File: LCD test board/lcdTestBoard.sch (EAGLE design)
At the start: 71 parts, among them CON2 AXE534124, U1 LP2980-ADJ, U2 ST2378E_TSSOP, U3 MCP1662, U4 TPS62260, U5 ST2378E_TSSOP, U6 LP2980-ADJ, U7 TPS62260, U8 LP2980-ADJ, U9 TPS62260

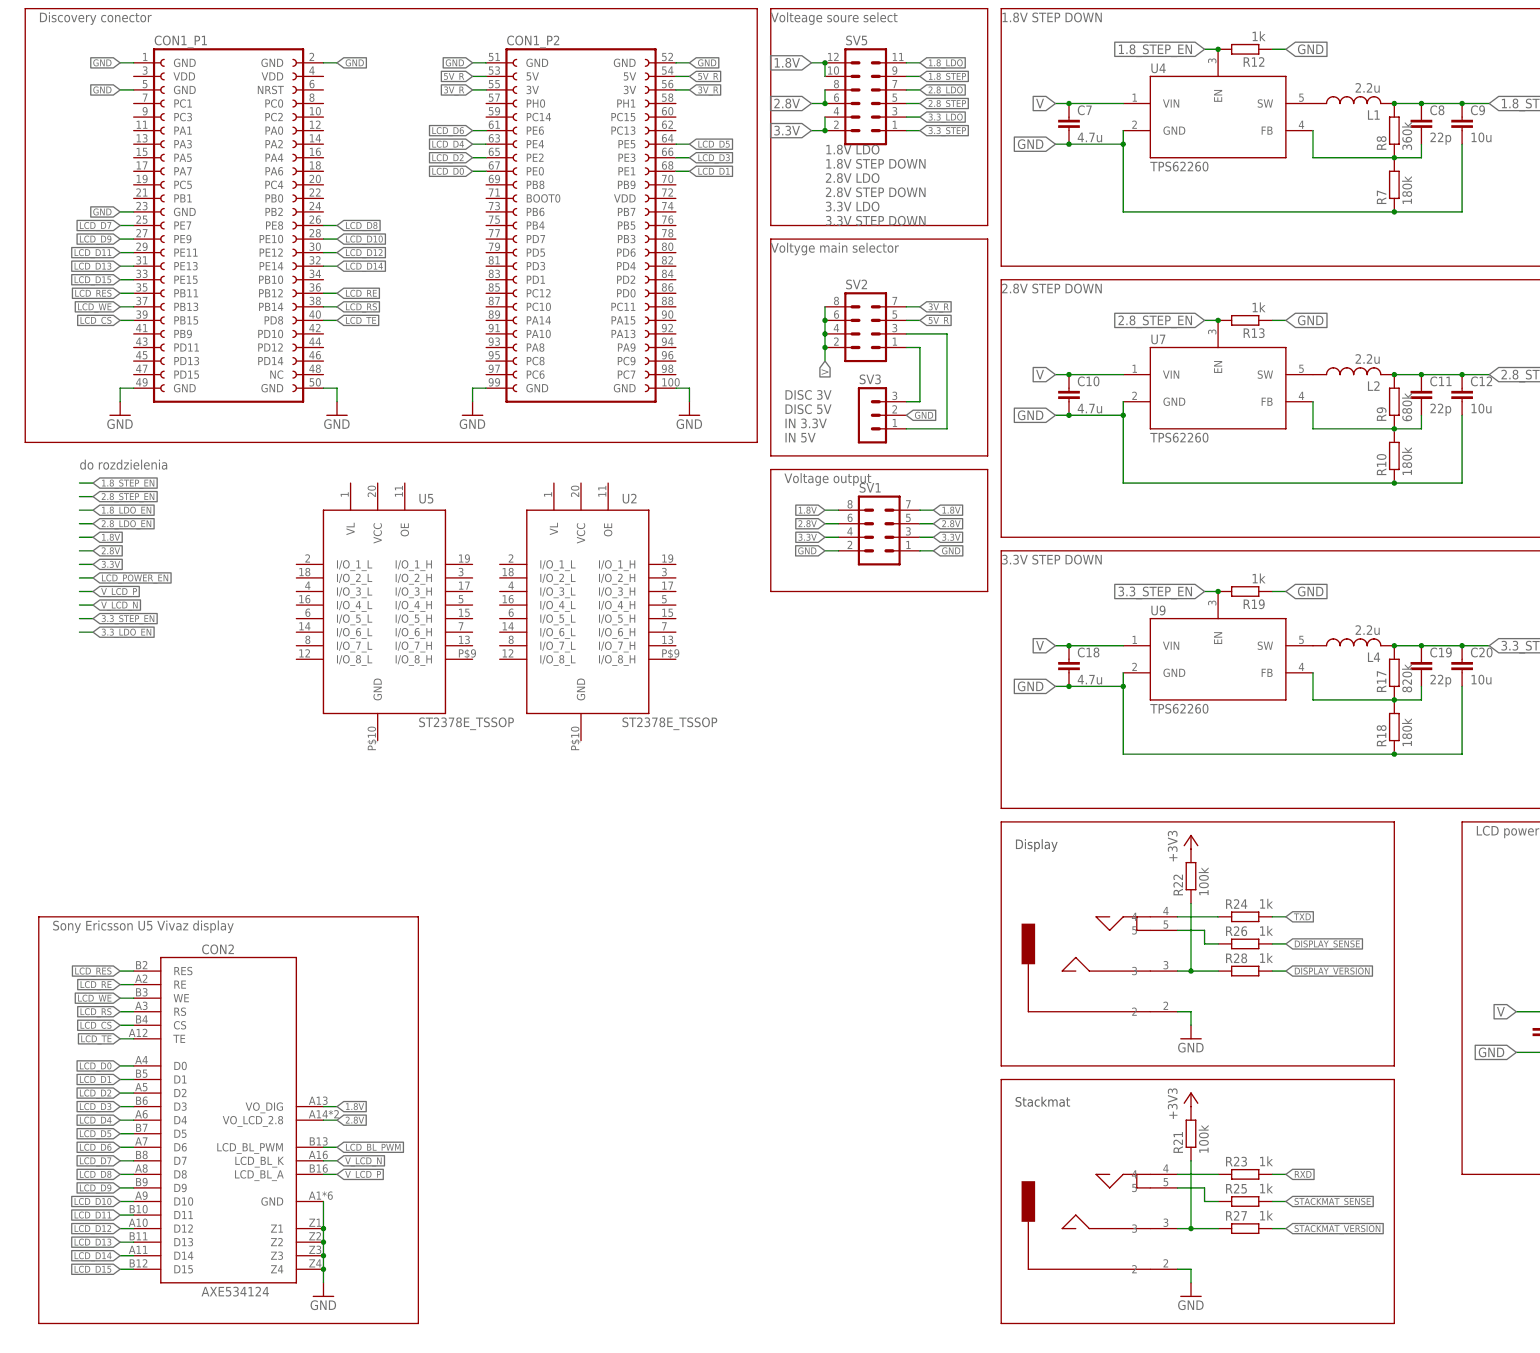
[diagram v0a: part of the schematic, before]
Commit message: polaczono wyswietlacz i stackmate do portu usart procesora, dodano invertery
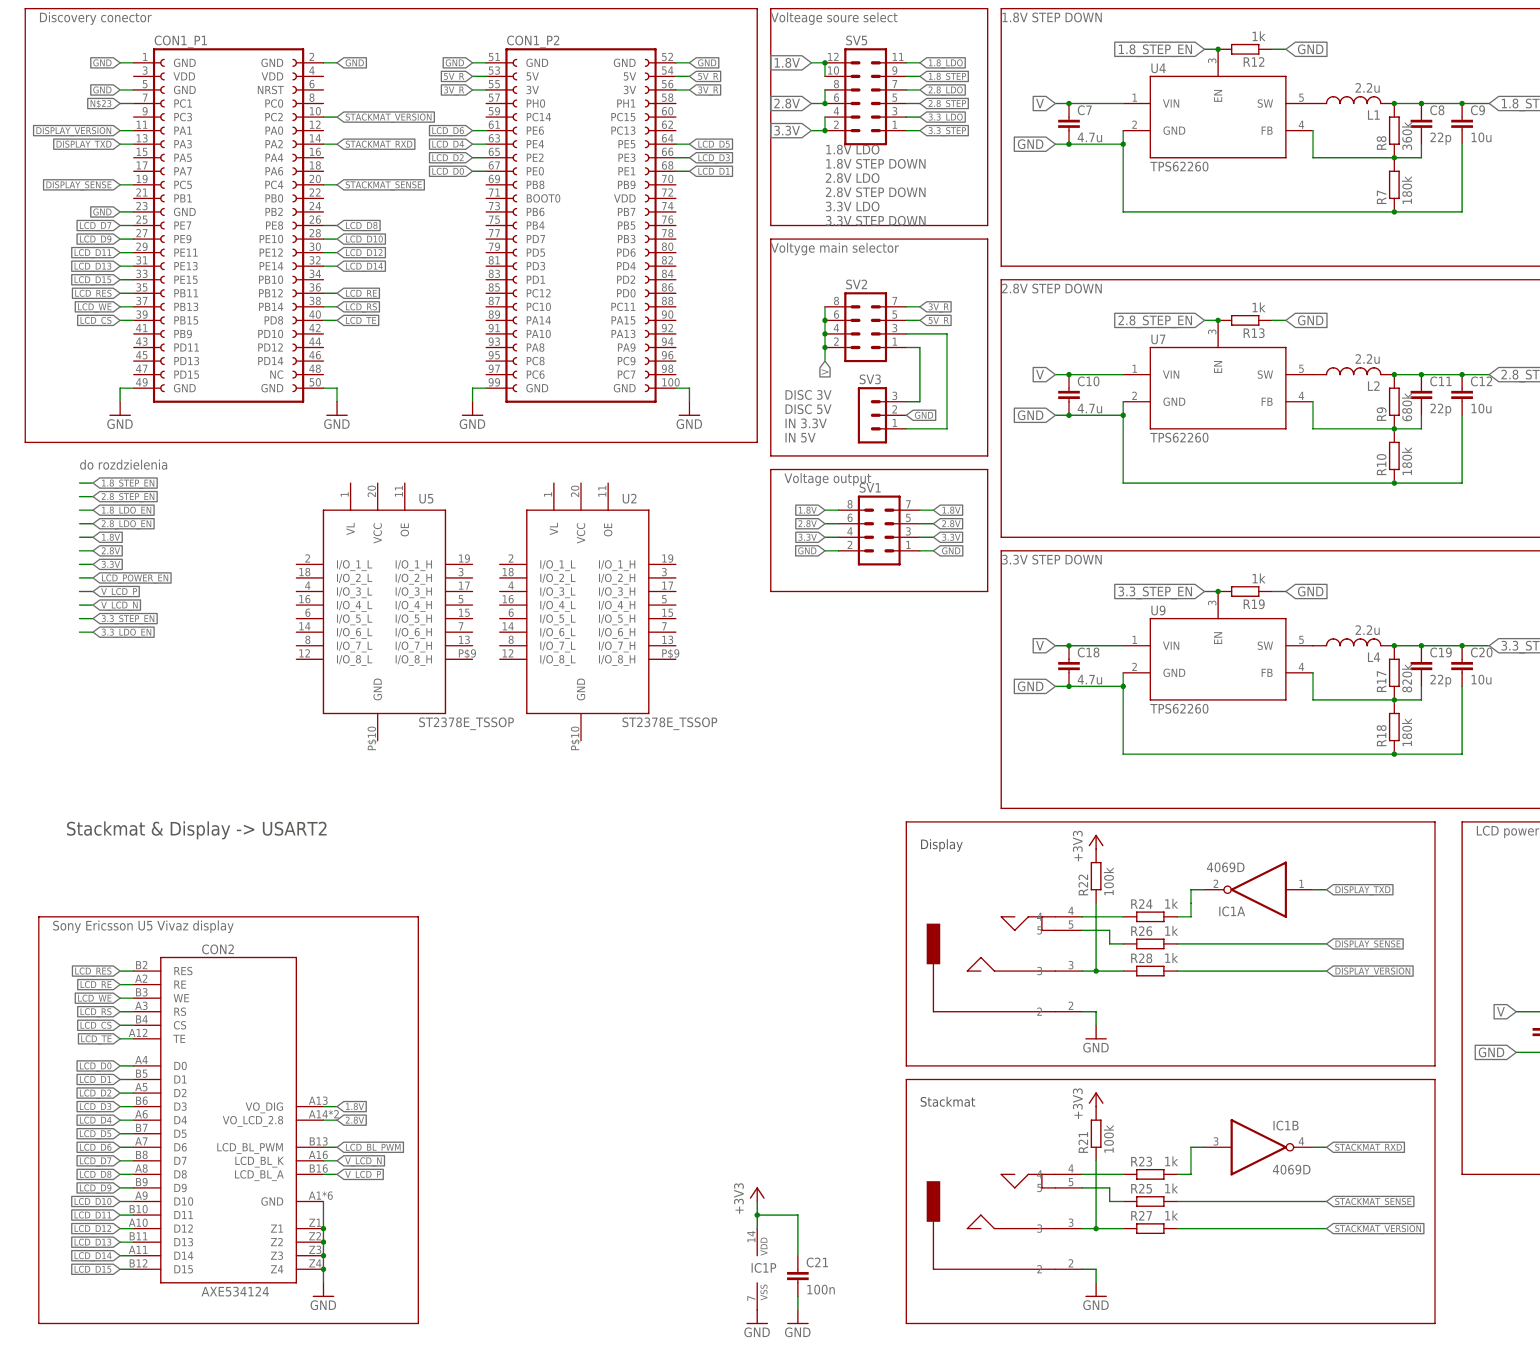
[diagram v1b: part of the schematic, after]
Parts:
- added C21: 100n, rcl:C-EUC0603K
- added IC1: 4069D, 40xx:4069D
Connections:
- removed net RXD: R23.1
- removed net TXD: R24.1
- new net DISPLAY_TXD: CON1_P1.PA3@13, IC1A.I
- new net N$20: IC1A.O, R24.1
- new net N$21: IC1B.I, R23.1
- new net N$23: CON1_P1.PC1@7
- new net STACKMAT_RXD: CON1_P1.PA2@14, IC1B.O
- net +3V3: now also C21.1, IC1P.VDD
- net DISPLAY_SENSE: now also CON1_P1.PC5@19
- net DISPLAY_VERSION: now also CON1_P1.PA1@11
- net GND: now also C21.2, IC1P.VSS
- net LCD_CS: now also CON1_P1.PB15@39
- net LCD_D0: now also CON1_P2.PE0@17
- net LCD_D1: now also CON1_P2.PE1@18
- net LCD_D10: now also CON1_P1.PE10@28
- net LCD_D11: now also CON1_P1.PE11@29
- net LCD_D12: now also CON1_P1.PE12@30
- net LCD_D13: now also CON1_P1.PE13@31
- net LCD_D14: now also CON1_P1.PE14@32
- net LCD_D15: now also CON1_P1.PE15@33
- net LCD_D2: now also CON1_P2.PE2@15
- net LCD_D3: now also CON1_P2.PE3@16
- net LCD_D4: now also CON1_P2.PE4@13
- net LCD_D5: now also CON1_P2.PE5@14
- net LCD_D6: now also CON1_P2.PE6@11
- net LCD_D7: now also CON1_P1.PE7@25
- net LCD_D8: now also CON1_P1.PE8@26
- net LCD_D9: now also CON1_P1.PE9@27
- net LCD_RE: now also CON1_P1.PB12@36
- net LCD_RES: now also CON1_P1.PB11@35
- net LCD_RS: now also CON1_P1.PB14@38
- net LCD_TE: now also CON1_P1.PD8@40
- net LCD_WE: now also CON1_P1.PB13@37
- net STACKMAT_SENSE: now also CON1_P1.PC4@20
- net STACKMAT_VERSION: now also CON1_P1.PC2@10
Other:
- note added: "Stackmat & Display -> USART2"
- moved on the sheet: R21, R22, R23, R24, R25, R26, R27, R28

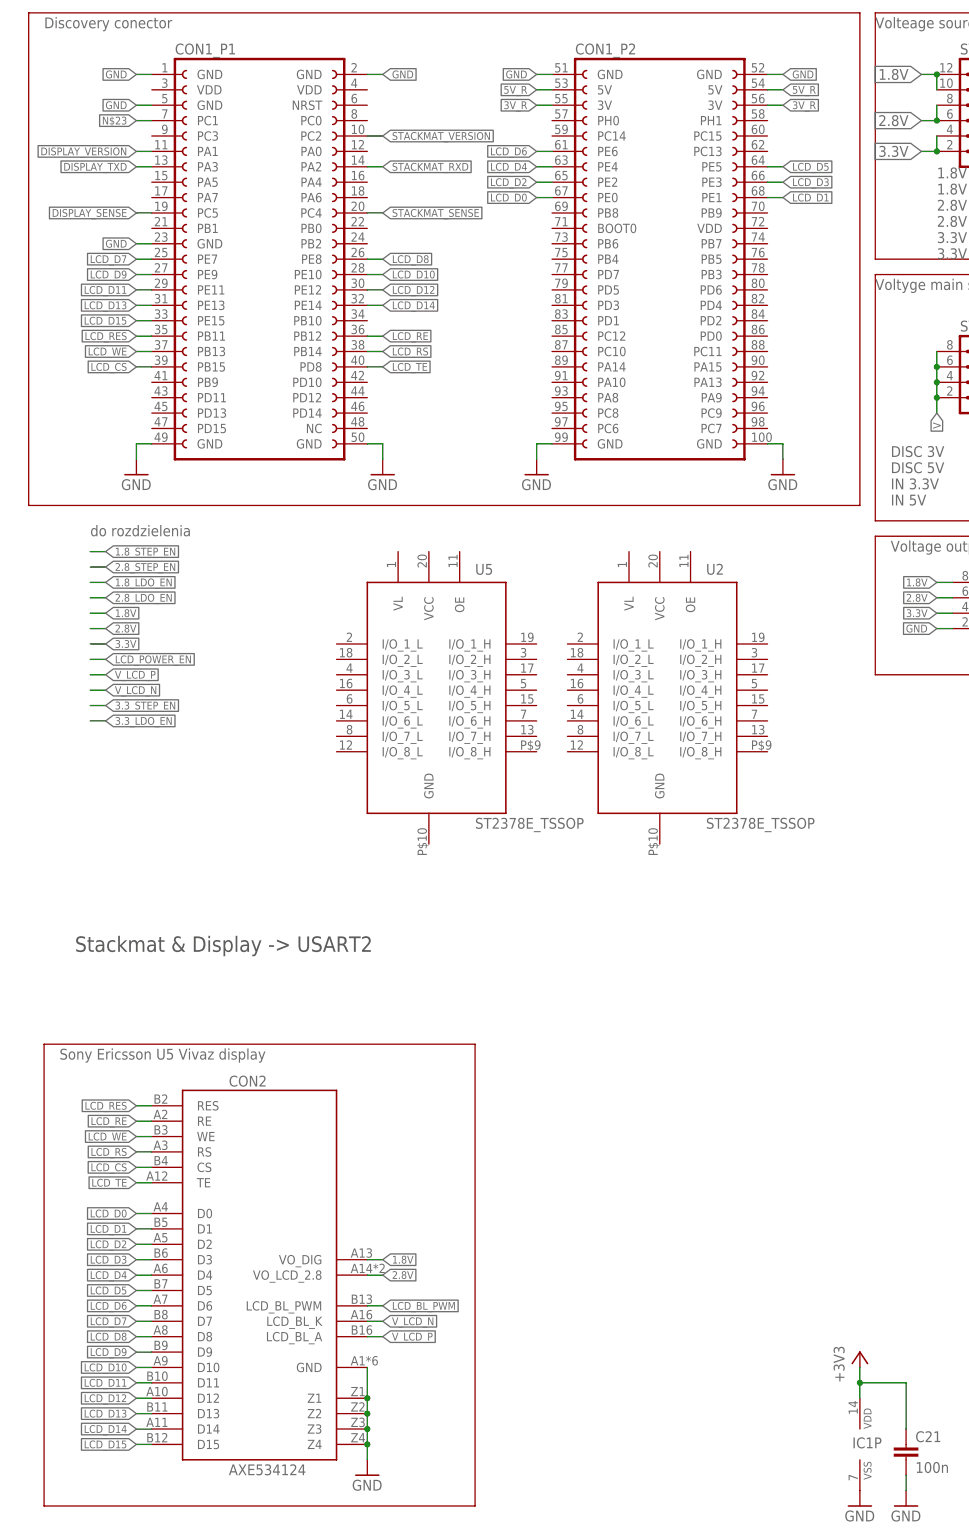
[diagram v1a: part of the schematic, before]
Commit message: dodano kondensatory przy złączu lcd
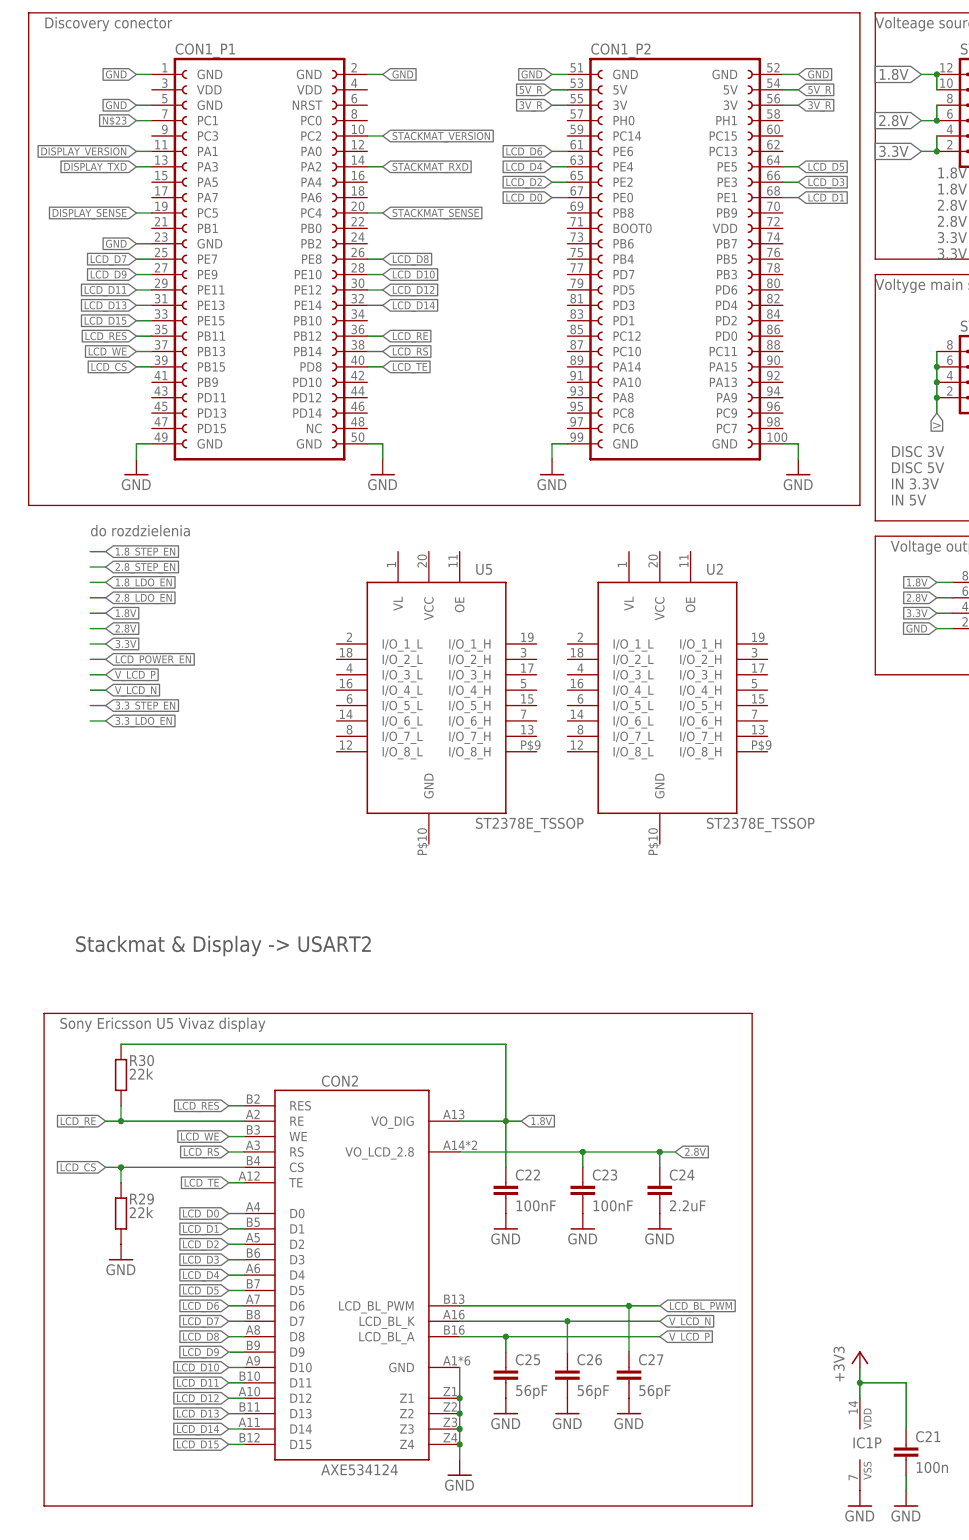
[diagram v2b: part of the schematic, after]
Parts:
- added C22, C23: 100nF, rcl:C-EUC0603K
- added C24: 2.2uF, rcl:C-EUC0603K
- added C25, C26, C27: 56pF, rcl:C-EUC0603K
- added R29, R30: 22k, rcl:R-EU_R0603
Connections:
- net 1.8V: now also C22.1, R30.1
- net 2.8V: now also C23.1, C24.1
- net GND: now also C22.2, C23.2, C24.2, C25.2, C26.2, C27.2, R29.2
- net LCD_BL_PWM: now also C27.1
- net LCD_CS: now also R29.1
- net LCD_RE: now also R30.2
- net V_LCD_N: now also C26.1
- net V_LCD_P: now also C25.1
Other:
- moved on the sheet: CON1_P2, CON2

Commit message: Update lcdTestBoard.sch
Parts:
- removed C13: 10u, rcl:C-EUC0603
- removed R17: 820k, rcl:R-EU_R0603
- removed R18: 180k, rcl:R-EU_R0603
- removed R19: 1k, rcl:R-EU_R0603
- removed U9: TPS62260, TPS6226x:TPS62260
- added U10: TPS63030DSKT, tps6303030:TPS63030DSKT
- C12, C14, C20, C9: device rcl:C-EUC0603 -> rcl:C-EUC1206
- C19: value 22p -> 10u
- L4: value 2.2u -> 1.5u
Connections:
- removed net LCD_POWER_EN: SV4.3
- net 2.8_STEP: now also C20.1; no longer C12.1
- net 3.3_STEP: now also C19.2, U10.FB, U10.VOUT; no longer C19.1, C20.1, L4.2, R17.2
- net 3.3_STEP_EN: now also C18.1, U10.EN; no longer R19.2, U9.EN
- net GND: now also C19.1, U10.GND, U10.PGND, U10.THERMALPAD; no longer C13.2, R18.1, R19.1, U9.GND
- net LCD_BL_PWM: now also SV4.3
- net N$6: now also U10.L2; no longer U9.SW
- net N$9: now also L4.2, U10.L1; no longer C19.2, R17.1, R18.2, U9.FB
- net V: now also C12.1, U10.PS/SYNC, U10.VIN, U10.VINA; no longer C14.1, C18.1, U9.VIN
- net V_LCD_P: now also C14.1; no longer C13.1
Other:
- moved on the sheet: C12, C14, C18, C19, C20, L4, U2, U5

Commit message: Update lcdTestBoard.sch
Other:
- note added: "Chips power lines"
- moved on the sheet: C1, C10, C11, C12, C14, C15, C16, C17, C18, C19, C2, C20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
